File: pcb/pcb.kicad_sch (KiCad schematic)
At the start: 0 parts

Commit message: basic usb schematics
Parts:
- added C1: 100n, symbol Device:C_Small
- added D1: D_TVS, symbol Device:D_TVS
- added F1: Fuse_Small, symbol Device:Fuse_Small
- added FB1, FB2: FerriteBead_Small, symbol Device:FerriteBead_Small
- added J1: USB_C_Receptacle_USB2.0_16P, symbol Connector:USB_C_Receptacle_USB2.0_16P
- added J2: Conn_01x04_Shielded, symbol Connector_Generic_Shielded:Conn_01x04_Shielded
- added R1, R2: 5k, symbol Device:R_Small
- added U1: nRF52840_moko_mk08, PCM_marbastlib-various:nRF52840_moko_mk08, symbol PCM_marbastlib-various:nRF52840_moko_mk08
- added U2: SRV05-4, Package_TO_SOT_SMD:SOT-23-6, symbol Power_Protection:SRV05-4
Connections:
- new net: F1.1, FB2.2
- new net: J1.A5 (CC1), R2.1
- new net: J1.B5 (CC2), R1.1
- new net +5V: F1.2, U2.5 (VP)
- new net GND: C1.2, D1.1 (A1), FB1.2, J2.4 (Pin_4), J2.SH (Shield), U2.2 (VN)
- new net GNDPWR: R1.2, R2.2
- new net GNDREF: C1.1, D1.2 (A2), FB1.1, J1.A1 (GND), J1.A12 (GND), J1.B1 (GND), J1.B12 (GND), J1.S1 (SHIELD)
- new net USB-D+: J1.A6 (D+), J1.B6 (D+), J2.3 (Pin_3), U2.6 (IO4)
- new net USB-D-: J1.A7 (D-), J1.B7 (D-), J2.2 (Pin_2), U2.1 (IO1)
- new net VBUS: FB2.1, J1.A4 (VBUS), J1.A9 (VBUS), J1.B4 (VBUS), J1.B9 (VBUS), J2.1 (Pin_1)

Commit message: schematic 1st draft
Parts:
- removed J2: Conn_01x04_Shielded, symbol Connector_Generic_Shielded:Conn_01x04_Shielded
- removed U1: nRF52840_moko_mk08, PCM_marbastlib-various:nRF52840_moko_mk08, symbol PCM_marbastlib-various:nRF52840_moko_mk08
- added C2: 4u7, symbol Device:C_Small
- added C3, C4: 10u, symbol Device:C_Polarized_Small
- added C5, C6: 1u, symbol Device:C_Small
- added C7, C8: 100n, symbol Device:C_Small
- added D2: LED_Small, symbol Device:LED_Small
- added J2: TC2030_SWD, PCM_marbastlib-various:CON_TC2030_outlined, symbol PCM_marbastlib-various:TC2030_SWD
- added J3: Conn_01x02_MountingPin, symbol Connector_Generic_MountingPin:Conn_01x02_MountingPin
- added J4: Conn_01x04_MountingPin, symbol Connector_Generic_MountingPin:Conn_01x04_MountingPin
- added R3: 1k5, symbol Device:R_Small
- added R4: 5k, symbol Device:R_Small
- added R5: 806k, symbol Device:R_Small
- added R6: 2M, symbol Device:R_Small
- added R7, R8: 5k1, symbol Device:R_Small
- added SW1: SW_SPDT, symbol Switch:SW_SPDT
- added SW2: RST, symbol Switch:SW_Push_45deg
- added SW3, SW4, SW5, SW6, SW7, SW8: Kailh_Choc, symbol Switch:SW_Push_45deg
- added U1: nRF52840_holyiot_18010, PCM_marbastlib-various:nRF52840_holyiot_18010, symbol PCM_marbastlib-various:nRF52840_holyiot_18010
- added U3: TP4056, Package_SO:SOP-8-1EP_4.57x4.57mm_P1.27mm_EP4.57x4.45mm, symbol PCM_marbastlib-various:TP4056
- added U4: XC6206PxxxMR, Package_TO_SOT_SMD:SOT-23-3, symbol Regulator_Linear:XC6206PxxxMR
- added U5: MAX17048, Package_DFN_QFN:DFN-8-1EP_2x2mm_P0.5mm_EP0.7x1.3mm, symbol PCM_marbastlib-various:MAX17048
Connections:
- net +5V: now also C2.1, C3.1, D2.2 (A), U1.22 (VBUS), U3.4 (VCC), U3.8 (CE)
- net GND: now also C2.2, C3.2, C4.2, C5.2, C6.2, C7.2, C8.2, J2.5 (GND), J3.2 (Pin_2), J3.MP (MountPin), J4.4 (Pin_4), J4.MP (MountPin), R4.2, R6.2, SW2.2, SW3.2, SW4.2, SW5.2, SW6.2, SW7.2, SW8.2, U1.1 (GND), U1.25 (GND), U1.37 (GND), U3.1 (TEMP), U3.3 (GND), U4.1 (GND), U5.1 (CTG), U5.4 (GND), U5.6 (QSTRT), U5.9 (GND)
- net USB-D+: now also J4.3 (Pin_3), U1.24 (D+)
- net USB-D-: now also J4.2 (Pin_2), U1.23 (D-)
- net VBUS: now also J4.1 (Pin_1)
- new net: R4.1, U3.2 (PROG)
- new net: R3.2, U3.7 (CHRG)
- new net: J3.1 (Pin_1), SW1.2 (B)
- new net: D2.1 (K), R3.1
- new net +3.3V: C6.1, C7.1, J2.1 (VCC), U1.14 (VDD_nRF), U4.2 (VO)
- new net +BATT: C4.1, C8.1, SW1.3 (C), U3.5 (BAT), U5.2 (CELL), U5.3 (VDD)
- new net +VSW: C5.1, R5.1, U4.3 (VI)
- new net ALERT: U5.5 (~{ALRT})
- new net RST: J2.3 (~{RST}), SW2.1, U1.21 (P0.18-RESET)
- new net SCL: R8.2, U1.13 (P0.05-A), U5.7 (SCL)
- new net SDA: R7.2, U1.15 (P0.07), U5.8 (SDA)
- new net SWDCLK: J2.4 (SWCLK), U1.31 (SWDCLK)
- new net SWDIO: J2.2 (SWDIO), U1.32 (SWDIO)
- new net VSENSE: R5.2, R6.1, U1.11 (P0.31-LF-A)
- new net sw3: SW3.1, U1.5 (P1.15-LF)
- new net sw4: SW4.1, U1.6 (P0.03-LF-A)
- new net sw5: SW5.1, U1.7 (P0.02-LF-A)
- new net sw6: SW6.1, U1.8 (P0.28-LF-A)
- new net sw7: SW7.1, U1.9 (P0.29-LF-A)
- new net sw8: SW8.1, U1.10 (P0.30-LF-A)

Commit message: remove unecessary battery voltage sensing circuitry
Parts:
- removed C8: 100n, symbol Device:C_Small
- removed R7, R8: 5k1, symbol Device:R_Small
- removed U5: MAX17048, Package_DFN_QFN:DFN-8-1EP_2x2mm_P0.5mm_EP0.7x1.3mm, symbol PCM_marbastlib-various:MAX17048
- C1, C2, C3, C4, C5, C6, C7: footprint (none) -> Capacitor_SMD:C_0603_1608Metric
- D1: footprint (none) -> Diode_SMD:D_SOD-123
- D2: footprint (none) -> LED_SMD:LED_SK6812MINI_PLCC4_3.5x3.5mm_P1.75mm
- F1: footprint (none) -> Fuse:Fuse_1206_3216Metric
- FB1, FB2: footprint (none) -> Capacitor_SMD:C_0402_1005Metric
- J1: footprint (none) -> Connector_USB:USB_C_Receptacle_HRO_TYPE-C-31-M-12
- J3: footprint (none) -> Connector_JST:JST_PH_S2B-PH-SM4-TB_1x02-1MP_P2.00mm_Horizontal
- J4: footprint (none) -> Connector_JST:JST_SH_SM04B-SRSS-TB_1x04-1MP_P1.00mm_Horizontal
- R1, R2: value 5k -> 5k1; footprint (none) -> Resistor_SMD:R_0603_1608Metric
- R3, R4, R5, R6: footprint (none) -> Resistor_SMD:R_0603_1608Metric
- SW3, SW4, SW5, SW6, SW7, SW8: footprint (none) -> PCM_marbastlib-choc:SW_choc_v1_HS_CPG135001S30_1u

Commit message: finish footprint assignment
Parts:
- SW1: footprint (none) -> Button_Switch_SMD:SW_SPDT_PCM12
- SW2: footprint (none) -> Button_Switch_THT:SW_PUSH_6mm_H4.3mm
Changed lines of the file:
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@@
 			)
 		)
-		(property "Footprint" ""
+		(property "Footprint" "Button_Switch_SMD:SW_SPDT_PCM12"
 			(at 228.6 137.16 0)
 			(effects
@@
 			)
 		)
-		(property "Footprint" ""
+		(property "Footprint" "Button_Switch_THT:SW_PUSH_6mm_H4.3mm"
 			(at 27.94 77.47 0)
 			(effects

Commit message: routing is hard
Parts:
- removed J2: TC2030_SWD, PCM_marbastlib-various:CON_TC2030_outlined, symbol PCM_marbastlib-various:TC2030_SWD
- removed J4: Conn_01x04_MountingPin, Connector_JST:JST_SH_SM04B-SRSS-TB_1x04-1MP_P1.00mm_Horizontal, symbol Connector_Generic_MountingPin:Conn_01x04_MountingPin
- added J4: Conn_02x03_Odd_Even, Connector_PinHeader_2.54mm:PinHeader_2x03_P2.54mm_Vertical, symbol Connector_Generic:Conn_02x03_Odd_Even
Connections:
- net +3.3V: now also J4.1 (Pin_1)
- net GND: now also J4.5 (Pin_5)
- net RST: now also J4.3 (Pin_3)
- net SWDCLK: now also J4.4 (Pin_4)
- net SWDIO: now also J4.2 (Pin_2)
- net SCL: no longer names the net of U1.13 (P0.05-A)
- net SDA: no longer names the net of U1.15 (P0.07)
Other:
- moved on the sheet: C1, C2, C3, C4, C5, C6, C7, D1, D2, F1, FB1, FB2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

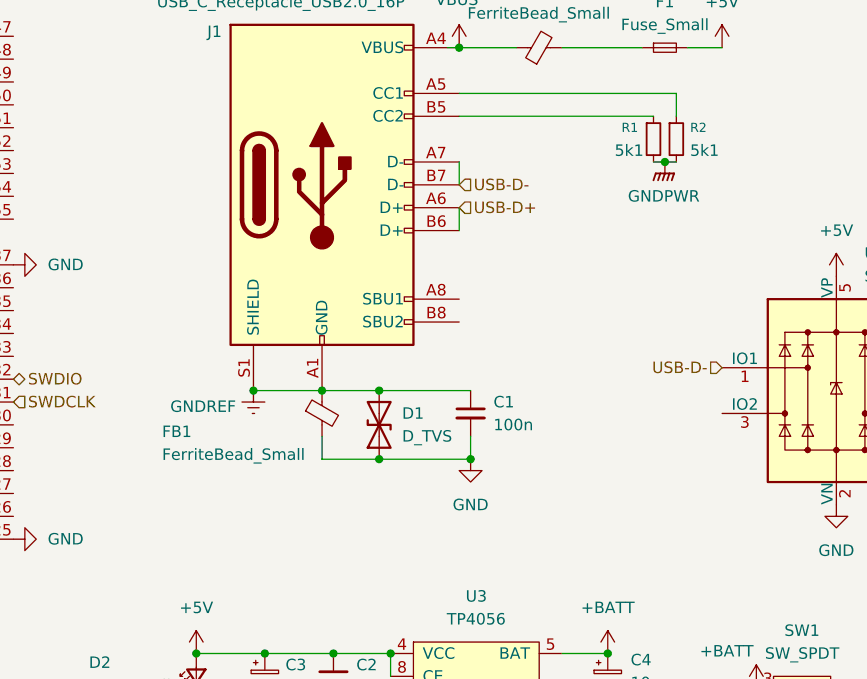
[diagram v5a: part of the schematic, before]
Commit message: one one gnd net, also get rid of some components
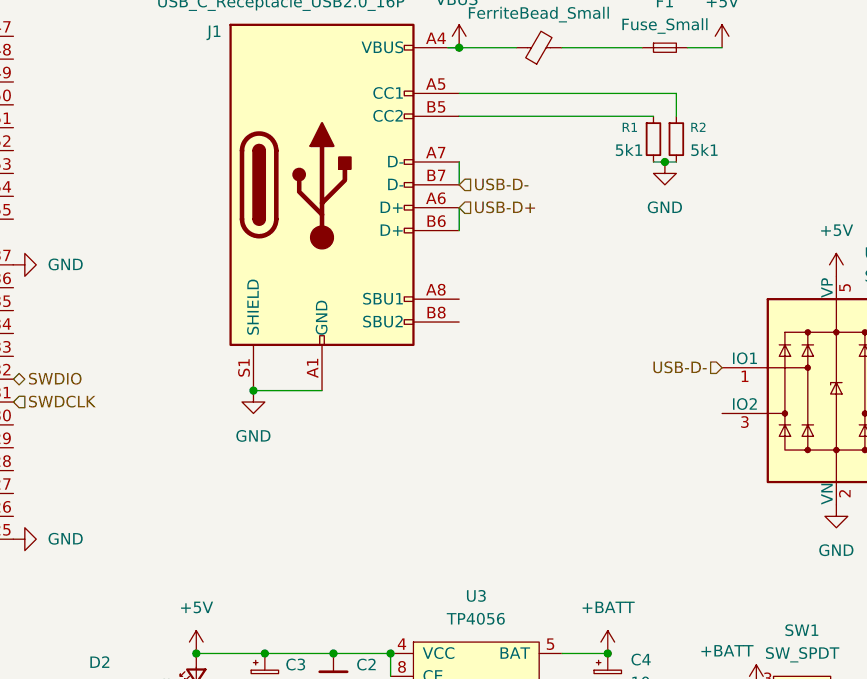
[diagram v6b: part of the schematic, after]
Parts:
- removed C1: 100n, Capacitor_SMD:C_0603_1608Metric, symbol Device:C_Small
- removed D1: D_TVS, Diode_SMD:D_SOD-123, symbol Device:D_TVS
- removed FB1: FerriteBead_Small, Capacitor_SMD:C_0402_1005Metric, symbol Device:FerriteBead_Small
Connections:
- net GNDPWR is gone; now on net GND: R1.2, R2.2
- net GNDREF is gone; now on net GND: J1.A1 (GND), J1.A12 (GND), J1.B1 (GND), J1.B12 (GND), J1.S1 (SHIELD)

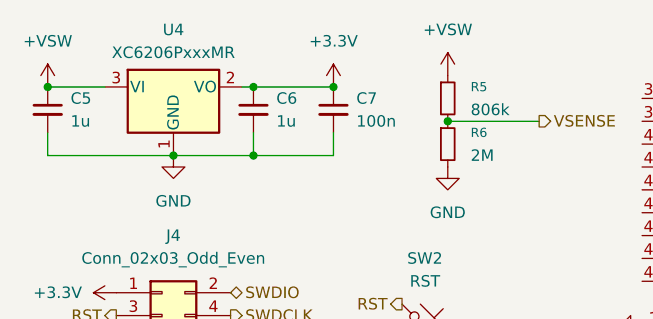
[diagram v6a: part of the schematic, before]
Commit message: finish routing 2nd draft
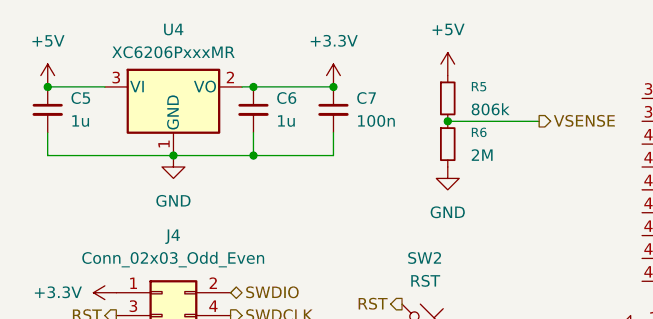
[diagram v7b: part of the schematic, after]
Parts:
- D2: footprint LED_SMD:LED_SK6812MINI_PLCC4_3.5x3.5mm_P1.75mm -> LED_SMD:LED_0603_1608Metric
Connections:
- net +VSW is gone; now on net +5V: C5.1, R5.1, U4.3 (VI)
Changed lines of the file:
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@@
+	)
+	(symbol
+		(lib_id "power:+5V")
+		(at 17.78 21.59 0)
+		(unit 1)
+		(exclude_from_sim no)
+		(in_bom yes)
+		(on_board yes)
+		(dnp no)
+		(fields_autoplaced yes)
+		(property "Reference" "#PWR05"
+			(at 17.78 25.4 0)
+			(effects
+				(font
+					(size 1.27 1.27)
+				)
+				(hide yes)
+			)
+		)
+		(property "Value" "+5V"
+			(at 17.78 16.51 0)
+			(effects
+				(font
+					(size 1.27 1.27)
+				)
+			)
+		)
+		(property "Footprint" ""
+			(at 17.78 21.59 0)
+			(effects
+				(font
+					(size 1.27 1.27)
+				)
+				(hide yes)
+			)
+		)
+		(property "Datasheet" ""
+			(at 17.78 21.59 0)
+			(effects
+				(font
+					(size 1.27 1.27)
+				)
+				(hide yes)
+			)
+		)
+		(property "Description" "Power symbol creates a global label with name \"+5V\""
+			(at 17.78 21.59 0)
+			(effects
+				(font
+					(size 1.27 1.27)
+				)
+				(hide yes)
+			)
+		)
+		(pin "1"
+		)
+		(instances
+			(project ""
+				(path "/ca7e7be3-8586-46b3-8a09-fe6a6c4a0309"
+					(reference "#PWR05")
+					(unit 1)
+				)
+			)
+		)
 	)
 	(symbol
@@
 	)
 	(symbol
-		(lib_id "power:+VSW")
-		(at 17.78 21.59 0)
-		(unit 1)
-		(exclude_from_sim no)
-		(in_bom yes)
-		(on_board yes)
-		(dnp no)
-		(fields_autoplaced yes)
-		(property "Reference" "#PWR022"
-			(at 17.78 25.4 0)
-			(effects
-				(font
-					(size 1.27 1.27)
-				)
-				(hide yes)
-			)
-		)
-		(property "Value" "+VSW"
-			(at 17.78 16.51 0)
-			(effects
-				(font
-					(size 1.27 1.27)
-				)
-			)
-		)
-		(property "Footprint" ""
-			(at 17.78 21.59 0)
-			(effects
-				(font
-					(size 1.27 1.27)
-				)
-				(hide yes)
-			)
-		)
-		(property "Datasheet" ""
-			(at 17.78 21.59 0)
-			(effects
-				(font
-					(size 1.27 1.27)
-				)
-				(hide yes)
-			)
-		)
-		(property "Description" "Power symbol creates a global label with name \"+VSW\""
-			(at 17.78 21.59 0)
-			(effects
-				(font
-					(size 1.27 1.27)
-				)
-				(hide yes)
-			)
-		)
-		(pin "1"
-		)
-		(instances
-			(project ""
-				(path "/ca7e7be3-8586-46b3-8a09-fe6a6c4a0309"
-					(reference "#PWR022")
-					(unit 1)
-				)
-			)
-		)
-	)
-	(symbol
 		(lib_id "power:+3.3V")
 		(at 93.98 92.71 180)
@@
 	)
 	(symbol
+		(lib_id "power:+5V")
+		(at 62.23 20.32 0)
+		(unit 1)
+		(exclude_from_sim no)
+		(in_bom yes)
+		(on_board yes)
+		(dnp no)
+		(fields_autoplaced yes)
+		(property "Reference" "#PWR022"
+			(at 62.23 24.13 0)
+			(effects
+				(font
+					(size 1.27 1.27)
+				)
+				(hide yes)
+			)
+		)
+		(property "Value" "+5V"
+			(at 62.23 15.24 0)
+			(effects
+				(font
+					(size 1.27 1.27)
+				)
+			)
+		)
+		(property "Footprint" ""
+			(at 62.23 20.32 0)
+			(effects
+				(font
+					(size 1.27 1.27)
+				)
+				(hide yes)
+			)
+		)
+		(property "Datasheet" ""
+			(at 62.23 20.32 0)
+			(effects
+				(font
+					(size 1.27 1.27)
+				)
+				(hide yes)
+			)
+		)
+		(property "Description" "Power symbol creates a global label with name \"+5V\""
+			(at 62.23 20.32 0)
+			(effects
+				(font
+					(size 1.27 1.27)
+				)
+				(hide yes)
+			)
+		)
+		(pin "1"
+		)
+		(instances
+			(project ""
+				(path "/ca7e7be3-8586-46b3-8a09-fe6a6c4a0309"
+					(reference "#PWR022")
+					(unit 1)
+				)
+			)
+		)
+	)
+	(symbol
 		(lib_id "power:GND")
 		(at 165.1 96.52 0)
@@
 	)
 	(symbol
-		(lib_id "power:+VSW")
-		(at 62.23 20.32 0)
-		(unit 1)
-		(exclude_from_sim no)
-		(in_bom yes)
-		(on_board yes)
-		(dnp no)
-		(fields_autoplaced yes)
-		(property "Reference" "#PWR028"
-			(at 62.23 24.13 0)
-			(effects
-				(font
-					(size 1.27 1.27)
-				)
-				(hide yes)
-			)
-		)
-		(property "Value" "+VSW"
-			(at 62.23 15.24 0)
-			(effects
-				(font
-					(size 1.27 1.27)
-				)
-			)
-		)
-		(property "Footprint" ""
-			(at 62.23 20.32 0)
-			(effects
-				(font
-					(size 1.27 1.27)
-				)
-				(hide yes)
-			)
-		)
-		(property "Datasheet" ""
-			(at 62.23 20.32 0)
-			(effects
-				(font
-					(size 1.27 1.27)
-				)
-				(hide yes)
-			)
-		)
-		(property "Description" "Power symbol creates a global label with name \"+VSW\""
-			(at 62.23 20.32 0)
-			(effects
-				(font
-					(size 1.27 1.27)
-				)
-				(hide yes)
-			)
-		)
-		(pin "1"
-		)
-		(instances
-			(project ""
-				(path "/ca7e7be3-8586-46b3-8a09-fe6a6c4a0309"
-					(reference "#PWR028")
-					(unit 1)
-				)
-			)
-		)
-	)
-	(symbol
 		(lib_id "Device:C_Small")
 		(at 40.64 24.13 0)
@@
 			)
 		)
-		(property "Footprint" "LED_SMD:LED_SK6812MINI_PLCC4_3.5x3.5mm_P1.75mm"
+		(property "Footprint" "LED_SMD:LED_0603_1608Metric"
 			(at 149.86 93.98 90)
 			(effects

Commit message: pcb v3 - 2 layers again
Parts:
- SW2: footprint Button_Switch_THT:SW_PUSH_6mm_H4.3mm -> horrortroll_lib:TS-1088R-02526
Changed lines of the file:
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@@
 			)
 		)
-		(property "Footprint" "Button_Switch_THT:SW_PUSH_6mm_H4.3mm"
+		(property "Footprint" "horrortroll_lib:TS-1088R-02526"
 			(at 59.69 48.26 0)
 			(effects
